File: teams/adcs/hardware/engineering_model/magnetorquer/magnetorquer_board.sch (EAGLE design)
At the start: 38 parts

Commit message: ADCS/MT: PCB revision
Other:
- moved on the sheet: JP1, JP2
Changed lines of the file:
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@@
 <?xml version="1.0" encoding="utf-8"?>
 <!DOCTYPE eagle SYSTEM "eagle.dtd">
-<eagle version="7.5.0">
+<eagle version="8.4.1">
 <drawing>
 <settings>
 <setting alwaysvectorfont="no"/>
+<setting keepoldvectorfont="yes"/>
 <setting verticaltext="up"/>
 </settings>
@@
 <instance part="C21" gate="G$1" x="-2.54" y="134.62"/>
 <instance part="GND27" gate="1" x="-2.54" y="142.24" rot="R180"/>
-<instance part="JP1" gate="G$1" x="71.12" y="182.88" rot="R270"/>
-<instance part="JP2" gate="G$1" x="104.14" y="160.02"/>
+<instance part="JP1" gate="G$1" x="71.12" y="185.42" rot="R270"/>
+<instance part="JP2" gate="G$1" x="93.98" y="162.56"/>
 </instances>
 <busses>
@@
 <pinref part="C3" gate="G$1" pin="1"/>
 <wire x1="48.26" y1="175.26" x2="58.42" y2="175.26" width="0.1524" layer="91"/>
-<wire x1="58.42" y1="175.26" x2="71.12" y2="175.26" width="0.1524" layer="91"/>
-<wire x1="71.12" y1="175.26" x2="73.66" y2="175.26" width="0.1524" layer="91"/>
-<wire x1="73.66" y1="175.26" x2="78.74" y2="175.26" width="0.1524" layer="91"/>
 <wire x1="48.26" y1="175.26" x2="48.26" y2="172.72" width="0.1524" layer="91"/>
 <junction x="48.26" y="175.26"/>
@@
 <wire x1="66.04" y1="170.18" x2="66.04" y2="167.64" width="0.1524" layer="91"/>
 <pinref part="JP1" gate="G$1" pin="1"/>
+<pinref part="JP1" gate="G$1" pin="2"/>
+<wire x1="58.42" y1="175.26" x2="71.12" y2="175.26" width="0.1524" layer="91"/>
+<wire x1="71.12" y1="175.26" x2="73.66" y2="175.26" width="0.1524" layer="91"/>
+<wire x1="73.66" y1="175.26" x2="78.74" y2="175.26" width="0.1524" layer="91"/>
+<wire x1="73.66" y1="177.8" x2="73.66" y2="175.26" width="0.1524" layer="91"/>
+<junction x="73.66" y="175.26"/>
+<wire x1="71.12" y1="177.8" x2="71.12" y2="175.26" width="0.1524" layer="91"/>
 <junction x="71.12" y="175.26"/>
-<pinref part="JP1" gate="G$1" pin="2"/>
-<junction x="73.66" y="175.26"/>
 </segment>
 </net>
@@
 </segment>
 <segment>
+<label x="111.76" y="165.1" size="1.778" layer="95" rot="R90" xref="yes"/>
+<pinref part="JP2" gate="G$1" pin="1"/>
 <pinref part="R4" gate="G$1" pin="1"/>
-<wire x1="111.76" y1="160.02" x2="111.76" y2="162.56" width="0.1524" layer="91"/>
-<label x="111.76" y="162.56" size="1.778" layer="95" rot="R90" xref="yes"/>
-<pinref part="JP2" gate="G$1" pin="1"/>
-<junction x="111.76" y="160.02"/>
-</segment>
-<segment>
+<wire x1="111.76" y1="165.1" x2="111.76" y2="162.56" width="0.1524" layer="91"/>
+<wire x1="111.76" y1="162.56" x2="111.76" y2="160.02" width="0.1524" layer="91"/>
+<wire x1="111.76" y1="162.56" x2="101.6" y2="162.56" width="0.1524" layer="91"/>
+<junction x="111.76" y="162.56"/>
+</segment>
+<segment>

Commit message: ADCS/MT: Update LDO and PC104 stack board
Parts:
- LDO_3V1, LDO_5V1: value LINEAR_LDO_LT1761-X -> TPS732XX; device DubSat1 Components:LINEAR_LDO_LT1761-X -> DubSat1 Components:TPS732XX
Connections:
- net GND: now also U$1.BDOT_GND@87; no longer U$1.BDOT_VBAT@86
- net VBAT: now also U$1.BDOT_VBAT@86; no longer U$1.BDOT_GND@87
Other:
- moved on the sheet: C6

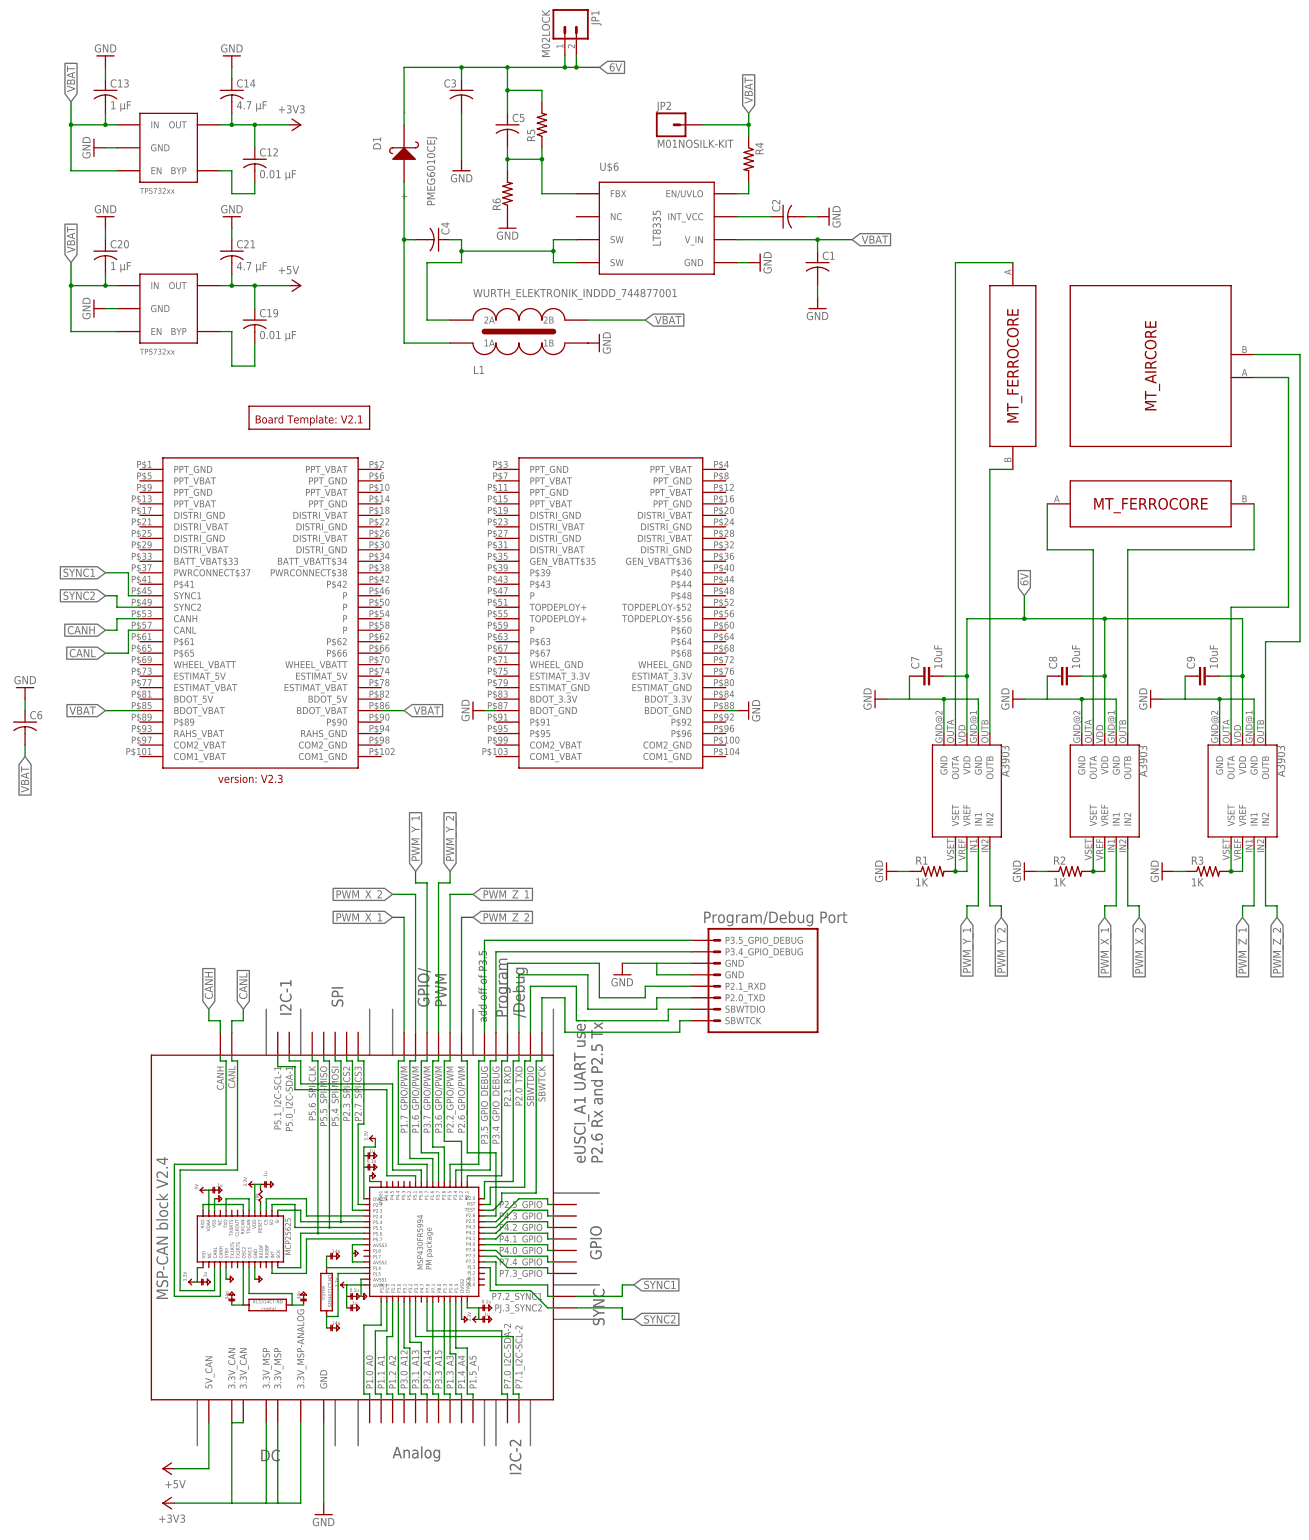
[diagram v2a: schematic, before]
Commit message: ADCS/MT: Reconnect to stack and use new SEPIC layout
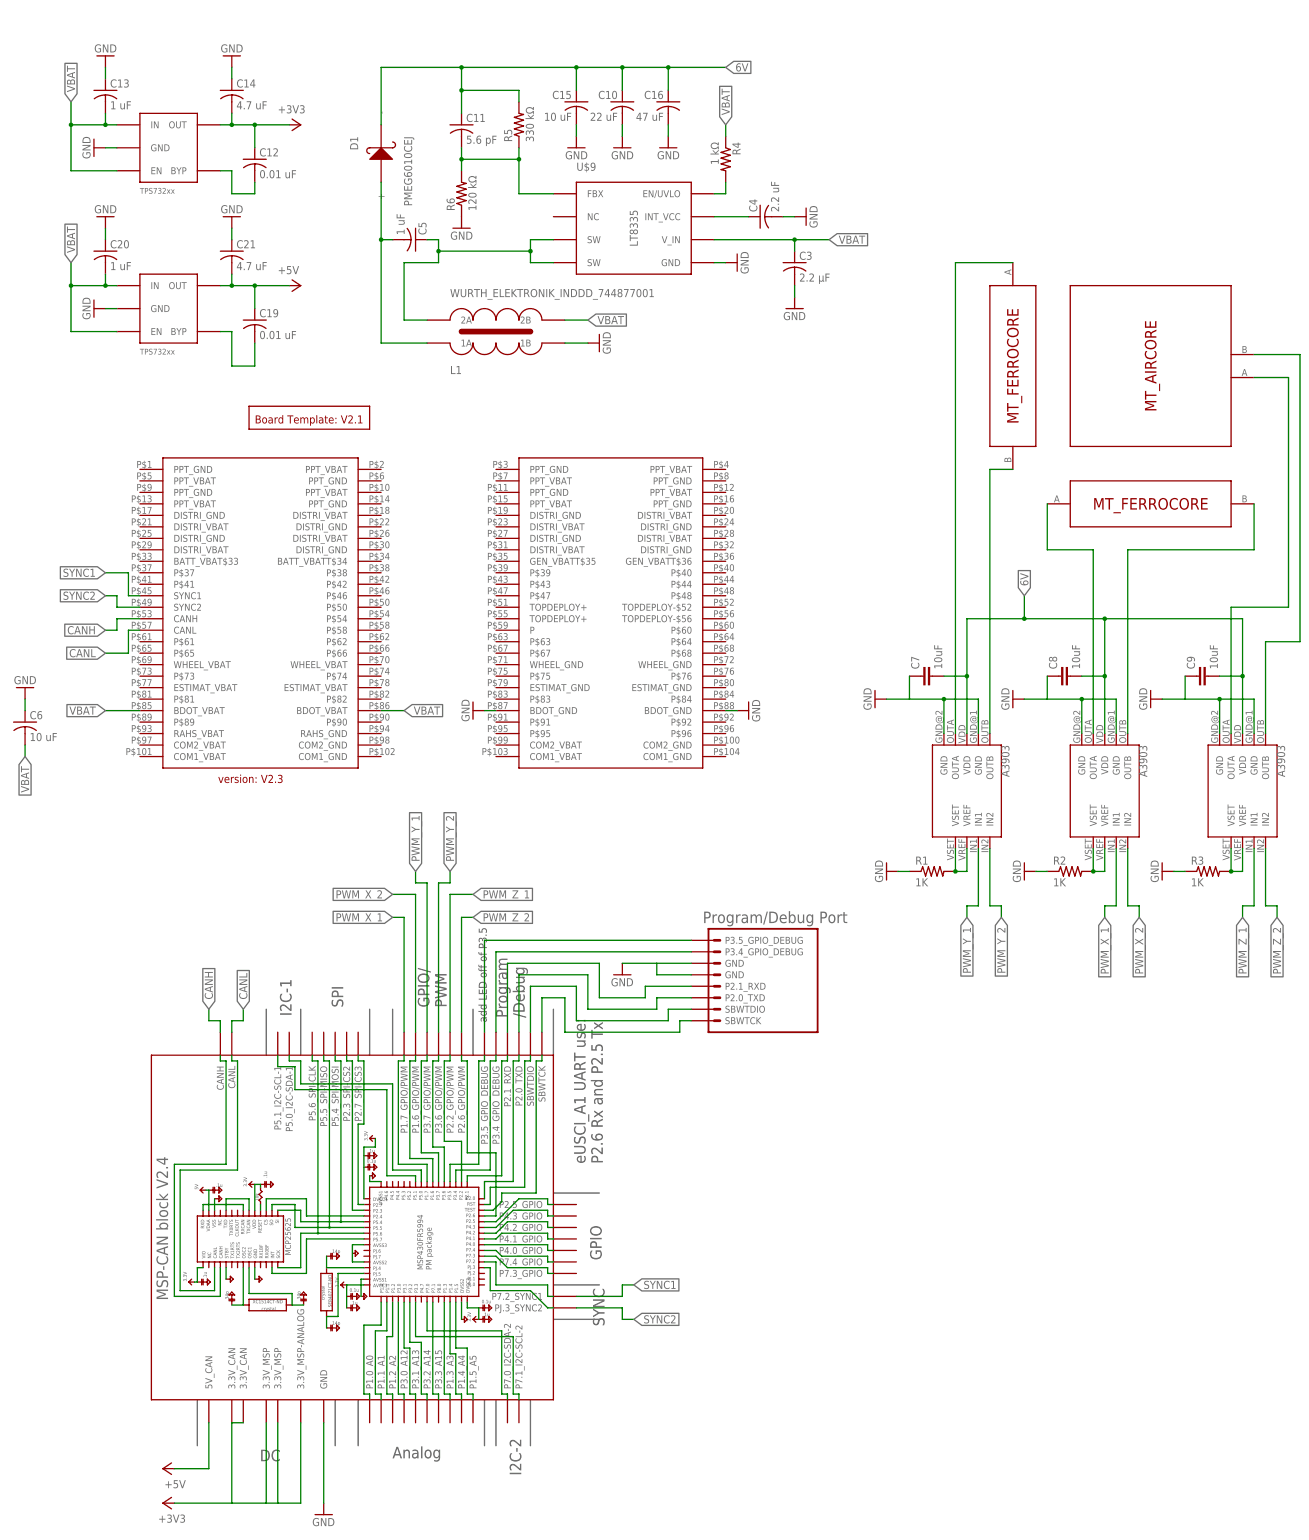
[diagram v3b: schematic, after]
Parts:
- removed C1, C2: (no value), rcl:C-USC0805
- removed JP1: M02LOCK, SparkFun-Connectors:M02LOCK
- removed JP2: M01NOSILK-KIT, SparkFun-Connectors:M01NOSILK-KIT
- removed U$6: LT8335, DubSat1 Components:LT8335
- added C10: 22 uF, rcl:C-USC1206
- added C11: 5.6 pF, rcl:C-USC0805
- added C15: 10 uF, rcl:C-USC0805
- added C16: 47 uF, rcl:C-USC1206
- added U$9: LT8335, DubSat1 Components:LT8335
- C12, C19: value 0.01 μF -> 0.01 uF
- C13, C20: value 1 μF -> 1 uF
- C14, C21: value 4.7 μF -> 4.7 uF
- C3: value (none) -> 2.2 μF
- C4: value (none) -> 2.2 uF
- C5: value (none) -> 1 uF
- C6: value (none) -> 10 uF
- R4: value (none) -> 1 kΩ; device rcl:R-US_R0805 -> DubSat1 Components:RESISTOR0805
- R5: value (none) -> 330 kΩ; device rcl:R-US_R0805 -> DubSat1 Components:RESISTOR0805
- R6: value (none) -> 120 kΩ; device rcl:R-US_R0805 -> DubSat1 Components:RESISTOR0805
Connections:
- removed net EN_UVLO: R4.2, U$6.EN/UVLO
- removed net N$6: C4.2, D1.+, L1.1A
- new net EN_UVLO1: R4.2, U$9.EN/UVLO
- new net VD: C5.2, D1.+, L1.1A
- net 6V: now also C10.1, C11.1, C15.1, C16.1; no longer C3.1, C5.1, JP1.1, JP1.2
- net FBX: now also C11.2, U$9.FBX; no longer C5.2, U$6.FBX
- net GND: now also C10.2, C15.2, C16.2, C4.2, U$9.GND; no longer C1.2, C2.2, U$6.GND
- net INT_VCC: now also C4.1, U$9.INT_VCC; no longer C2.1, U$6.INT_VCC
- net SW: now also C5.1, U$9.SW@1, U$9.SW@2; no longer C4.1, U$6.SW@1, U$6.SW@2
- net VBAT: now also C3.1, U$9.V_IN; no longer C1.1, JP2.1, U$6.V_IN
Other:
- moved on the sheet: C3, C4, C5, D1, L1, R4, R5, R6

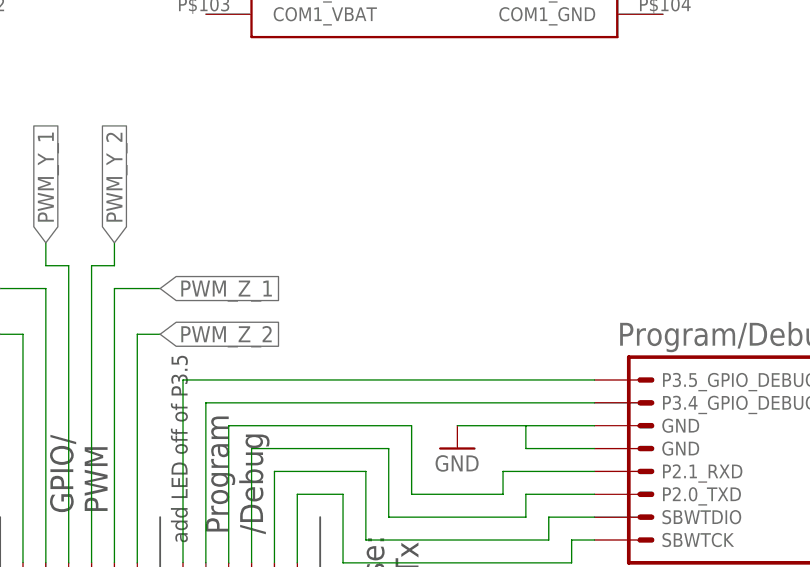
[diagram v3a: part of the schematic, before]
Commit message: ADCS/MT: Add LED to GPIO 3.5
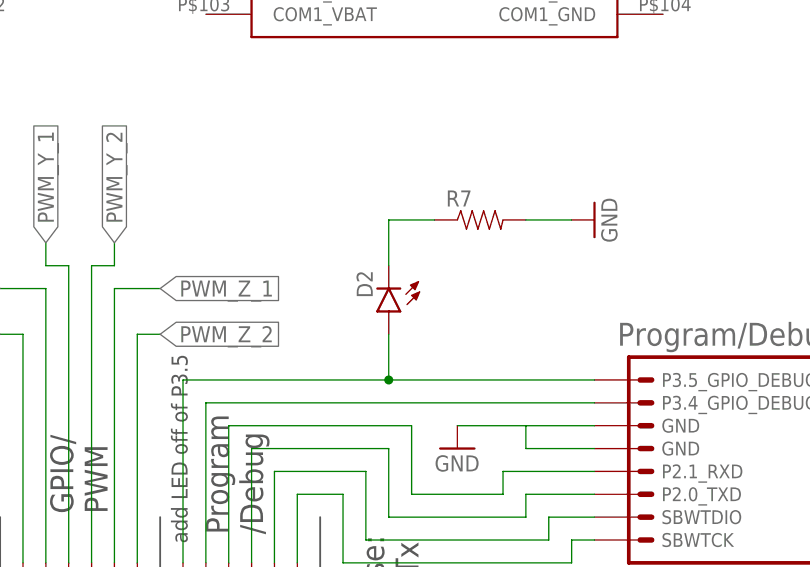
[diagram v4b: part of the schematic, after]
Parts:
- added D2: (no value), DubSat1 Components:LED
- added R7: (no value), DubSat1 Components:RESISTOR0805
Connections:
- new net N$3: D2.C, R7.1
- net GND: now also R7.2
- net N$32: now also D2.A
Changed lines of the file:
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@@
 <?xml version="1.0" encoding="utf-8"?>
 <!DOCTYPE eagle SYSTEM "eagle.dtd">
-<eagle version="8.4.3">
+<eagle version="8.5.2">
 <drawing>
 <settings>
@@
 <part name="C16" library="rcl" library_urn="urn:adsk.eagle:library:334" deviceset="C-US" device="C1206" package3d_urn="urn:adsk.eagle:package:23618/2" value="47 uF"/>
 <part name="GND32" library="supply1" library_urn="urn:adsk.eagle:library:371" deviceset="GND" device=""/>
+<part name="D2" library="DubSat1 Components" deviceset="LED" device=""/>
+<part name="R7" library="DubSat1 Components" deviceset="RESISTOR" device="0805"/>
+<part name="GND7" library="supply1" library_urn="urn:adsk.eagle:library:371" deviceset="GND" device=""/>
 </parts>
 <sheets>
@@
 <instance part="C16" gate="G$1" x="93.98" y="167.64" rot="MR0"/>
 <instance part="GND32" gate="1" x="93.98" y="157.48" rot="MR0"/>
+<instance part="D2" gate="G$1" x="76.2" y="-10.16" rot="R180"/>
+<instance part="R7" gate="G$1" x="86.36" y="0"/>
+<instance part="GND7" gate="1" x="99.06" y="0" rot="R90"/>
 </instances>
 <busses>
@@
 <pinref part="GND32" gate="1" pin="GND"/>
 <wire x1="93.98" y1="162.56" x2="93.98" y2="160.02" width="0.1524" layer="91"/>
+</segment>
+<segment>
+<pinref part="R7" gate="G$1" pin="2"/>
+<pinref part="GND7" gate="1" pin="GND"/>
+<wire x1="91.44" y1="0" x2="96.52" y2="0" width="0.1524" layer="91"/>
 </segment>
 </net>
@@
 <pinref part="U$7" gate="G$1" pin="P3.5_GPIO_DEBUG"/>
 <wire x1="53.34" y1="-38.1" x2="53.34" y2="-17.78" width="0.1524" layer="91"/>
-<wire x1="53.34" y1="-17.78" x2="99.06" y2="-17.78" width="0.1524" layer="91"/>
+<wire x1="53.34" y1="-17.78" x2="76.2" y2="-17.78" width="0.1524" layer="91"/>
 <pinref part="U$8" gate="G$1" pin="P3.5_GPIO_DEBUG"/>
+<pinref part="D2" gate="G$1" pin="A"/>
+<wire x1="76.2" y1="-17.78" x2="99.06" y2="-17.78" width="0.1524" layer="91"/>
+<wire x1="76.2" y1="-17.78" x2="76.2" y2="-12.7" width="0.1524" layer="91"/>
+<junction x="76.2" y="-17.78"/>
 </segment>
 </net>
@@
 </segment>
 </net>
+<net name="N$3" class="0">
+<segment>
+<pinref part="D2" gate="G$1" pin="C"/>
+<pinref part="R7" gate="G$1" pin="1"/>
+<wire x1="76.2" y1="-5.08" x2="76.2" y2="0" width="0.1524" layer="91"/>
+<wire x1="76.2" y1="0" x2="81.28" y2="0" width="0.1524" layer="91"/>
+</segment>
+</net>
